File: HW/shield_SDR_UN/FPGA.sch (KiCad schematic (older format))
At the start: 0 parts

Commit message: Se añade el esquema de la FPGA
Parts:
- added C? (x18): 0.1uF, symbol Device:C
- added C? (x10): 4.7uF, symbol Device:C
- added D?: LED, symbol Device:LED
- added J?: Conn_02x18_Counter_Clockwise, symbol Connector_Generic:Conn_02x18_Counter_Clockwise
- added R?: R, symbol Device:R
- added U?: 6SLX9TQG144, symbol 6slx9tqg144:6SLX9TQG144
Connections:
- net labels added: +1V2, +3.3V, ADDR_DATA_MCU, ADD_DAT_00, ADD_DAT_01, ADD_DAT_02, ADD_DAT_03, ADD_DAT_04, ADD_DAT_05, ADD_DAT_06, ADD_DAT_07, ADD_DAT_08, ADD_DAT_09, ADD_DAT_10, ADD_DAT_11, ADD_DAT_12, ADD_DAT_13, ADD_DAT_14, ADD_DAT_15, ADD_DAT_16, ADD_DAT_17, ADD_DAT_18, ADD_DAT_19, ADD_DAT_20, ADD_DAT_21, ADD_DAT_22, ADD_DAT_23, ADD_DAT_24, ADD_DAT_25, ADD_DAT_26, ADD_DAT_27, ADD_DAT_28, ADD_DAT_29, ADD_DAT_30, ADD_DAT_31, BLK_LED, CLK_INPUT, CTRL_MCU, FPGA_GPIO_00, FPGA_GPIO_01, FPGA_GPIO_02, FPGA_GPIO_03, FPGA_GPIO_04, FPGA_GPIO_05, FPGA_GPIO_06, FPGA_GPIO_07, FPGA_GPIO_08, FPGA_GPIO_09, FPGA_GPIO_10, FPGA_GPIO_11, FPGA_GPIO_12, FPGA_GPIO_13, FPGA_GPIO_14, FPGA_GPIO_15, FPGA_GPIO_16, FPGA_GPIO_17, FPGA_GPIO_18, FPGA_GPIO_19, FPGA_GPIO_20, FPGA_GPIO_21, FPGA_GPIO_22, FPGA_GPIO_23, FPGA_GPIO_24, FPGA_GPIO_25, FPGA_GPIO_26, FPGA_GPIO_27, FPGA_GPIO_28, FPGA_GPIO_29, FPGA_GPIO_30, FPGA_GPIO_31, GND, SCL_I2C, SDA_I2C, START_MCU, TCK_FPGA, TDI_FPGA, TDO_FPGA, TMS_FPGA
- wire segments 0 -> 290
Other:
- note added: "Blink LED"
- note added: "Bus de datos y dirección\npara comunicación con\nel MCU"
- note added: "Espacio para memoria\n(si se requiere)"
- note added: "FPGA"
- note added: "Pines GPIO"

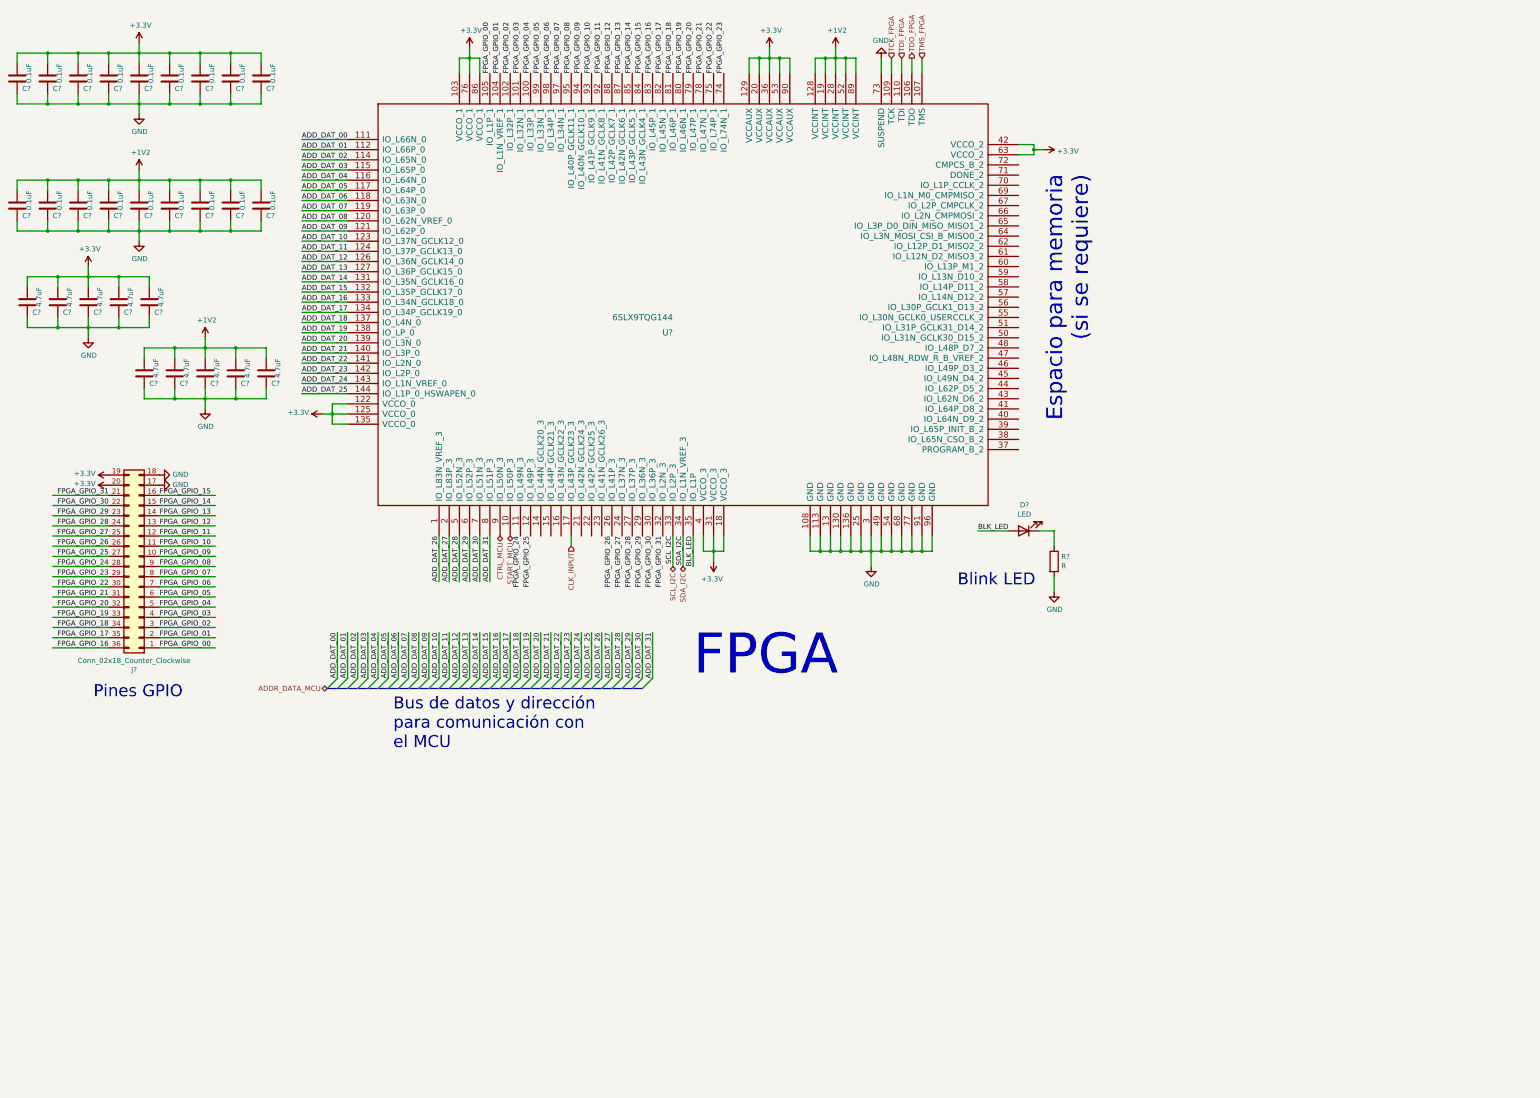
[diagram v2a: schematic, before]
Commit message: FPGA-ADC connection
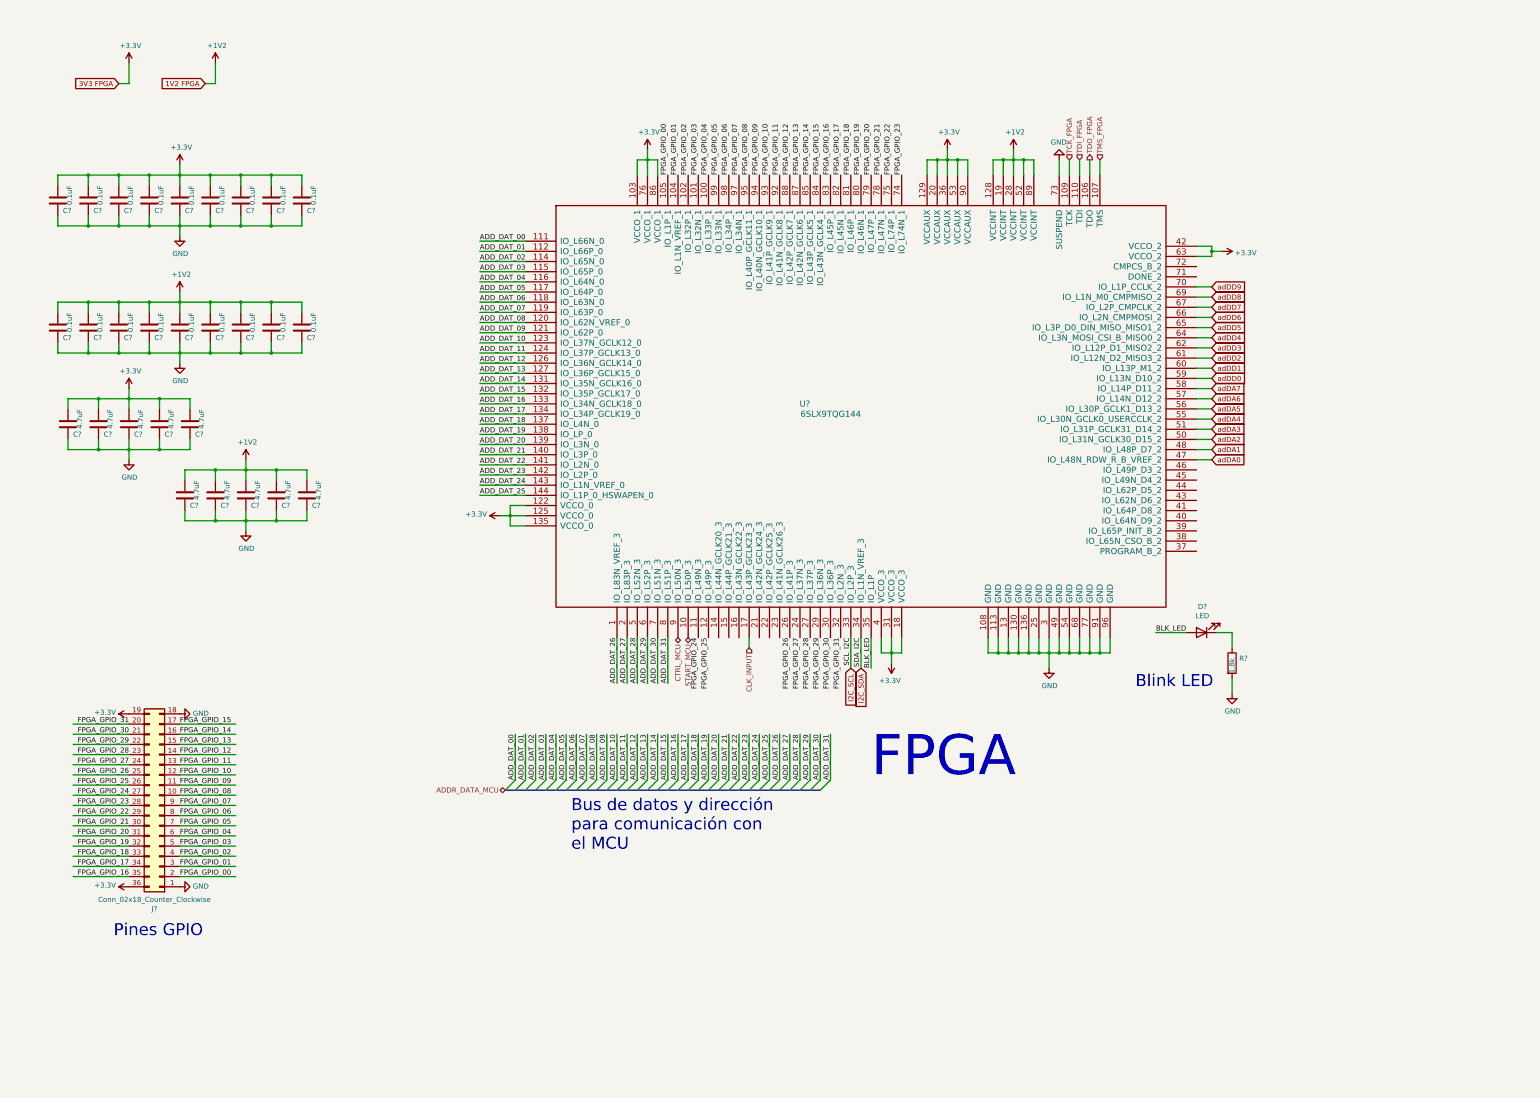
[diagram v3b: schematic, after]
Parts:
- R?: value R -> 1.8k
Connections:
- net labels added: 1V2 FPGA, 3V3 FPGA, I2C_SCL, I2C_SDA, adDA0, adDA1, adDA2, adDA3, adDA4, adDA5, adDA6, adDA7, adDD0, adDD1, adDD2, adDD3, adDD4, adDD5, adDD6, adDD7, adDD8, adDD9
- wire segments 290 -> 312
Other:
- note removed: "Espacio para memoria\n(si se requiere)"
- moved on the sheet: C?, D?, J?, R?, U?

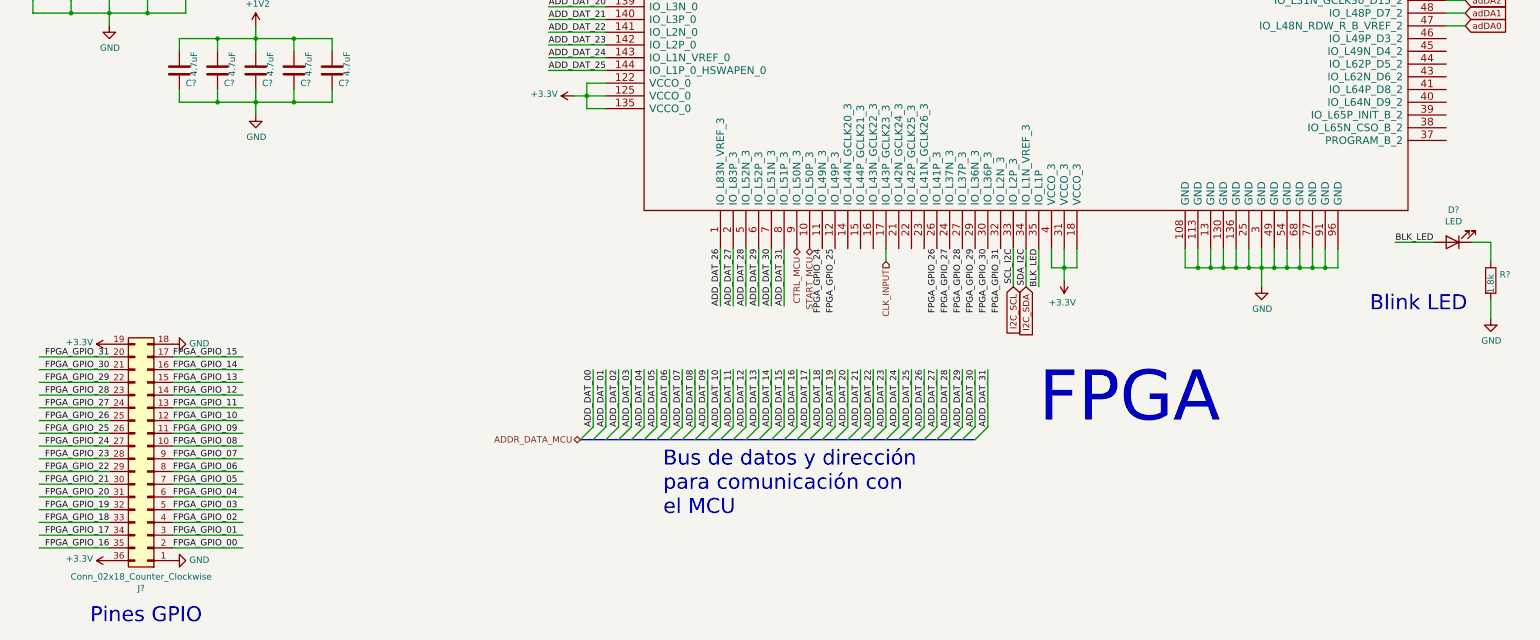
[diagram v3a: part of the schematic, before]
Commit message: STM32 connection updated
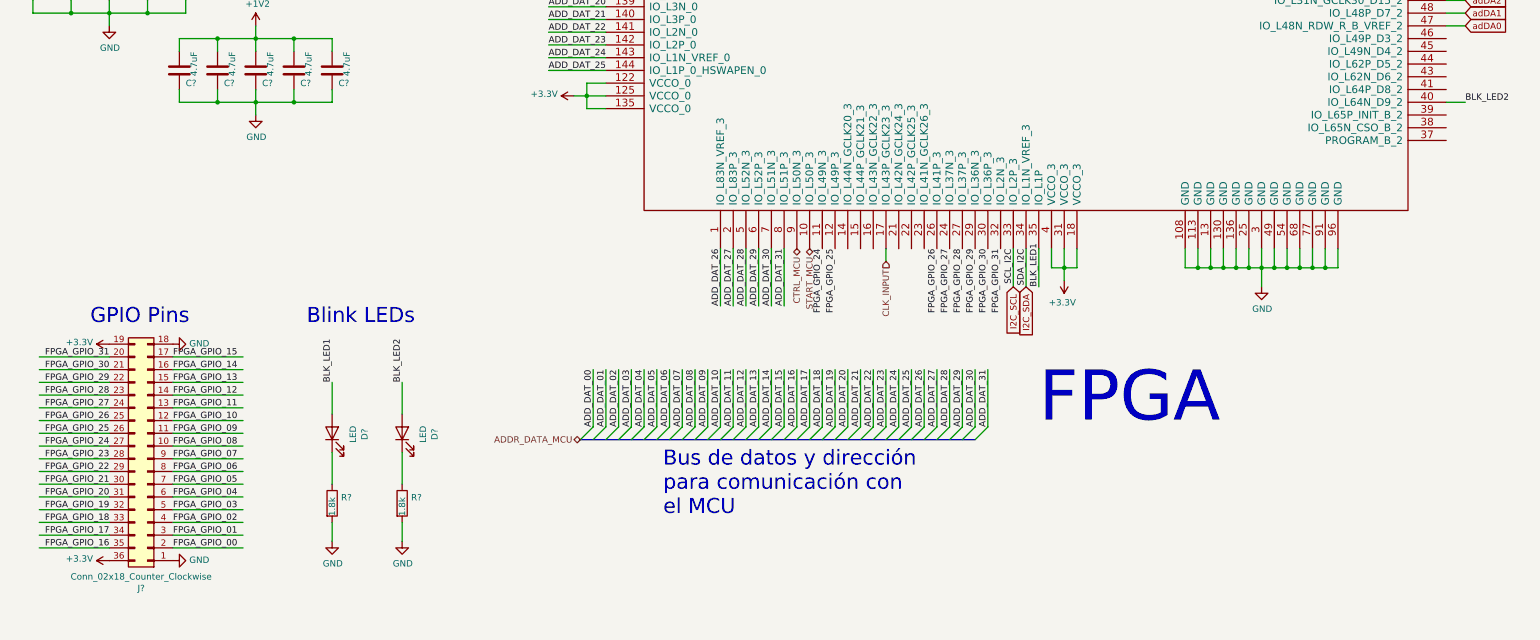
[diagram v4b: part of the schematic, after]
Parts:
- removed D?: LED, symbol Device:LED
- added D? (x2): LED, symbol Device:LED
- added R?: 1.8k, symbol Device:R
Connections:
- net labels added: BLK_LED1, BLK_LED2
- net labels removed: BLK_LED
- wire segments 312 -> 315
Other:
- note added: "Blink LEDs"
- note added: "GPIO Pins"
- note removed: "Blink LED"
- note removed: "Pines GPIO"
- moved on the sheet: R?
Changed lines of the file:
@@
 Text Label 8900 6650 3    50   ~ 0
 SDA_I2C
-Text Label 9000 6650 3    50   ~ 0
-BLK_LED
 Wire Wire Line
 	9000 6650 9000 6950
-Wire Wire Line
-	11800 6600 12100 6600
-$Comp
-L Device:LED D?
-U 1 1 5D3F3423
-P 12250 6600
-F 0 "D?" H 12242 6345 50  0000 C CNN
-F 1 "LED" H 12242 6436 50  0000 C CNN
-F 2 "" H 12250 6600 50  0001 C CNN
-F 3 "~" H 12250 6600 50  0001 C CNN
-	1    12250 6600
-	-1   0    0    1
-$EndComp
 $Comp
 L Device:R R?
 U 1 1 5D3F355A
-P 12550 6900
-F 0 "R?" H 12620 6946 50  0000 L CNN
-F 1 "1.8k" V 12550 6800 50  0000 L CNN
-F 2 "" V 12480 6900 50  0001 C CNN
-F 3 "~" H 12550 6900 50  0001 C CNN
-	1    12550 6900
-	1    0    0    -1
-$EndComp
-Wire Wire Line
-	12550 6750 12550 6600
-Wire Wire Line
-	12400 6600 12550 6600
+P 3450 8650
+F 0 "R?" H 3520 8696 50  0000 L CNN
+F 1 "1.8k" V 3450 8550 50  0000 L CNN
+F 2 "" V 3380 8650 50  0001 C CNN
+F 3 "~" H 3450 8650 50  0001 C CNN
+	1    3450 8650
+	1    0    0    -1
+$EndComp
 $Comp
 L power:GND #PWR?
 U 1 1 5D40658F
-P 12550 7200
-F 0 "#PWR?" H 12550 6950 50  0001 C CNN
-F 1 "GND" H 12555 7027 50  0000 C CNN
-F 2 "" H 12550 7200 50  0001 C CNN
-F 3 "" H 12550 7200 50  0001 C CNN
-	1    12550 7200
-	1    0    0    -1
-$EndComp
-Wire Wire Line
-	12550 7050 12550 7200
-Text Label 12100 6600 2    50   ~ 0
-BLK_LED
+P 3450 8950
+F 0 "#PWR?" H 3450 8700 50  0001 C CNN
+F 1 "GND" H 3455 8777 50  0000 C CNN
+F 2 "" H 3450 8950 50  0001 C CNN
+F 3 "" H 3450 8950 50  0001 C CNN
+	1    3450 8950
+	1    0    0    -1
+$EndComp
+Wire Wire Line
+	3450 8800 3450 8950
+Text Label 3450 7700 1    50   ~ 0
+BLK_LED1
 Wire Wire Line
 	8900 6650 8900 6950
@@
 Text Notes 9000 8050 0    394  ~ 0
 FPGA
-Text Notes 11600 7150 0    118  ~ 0
-Blink LED
+Text Notes 3250 7250 0    118  ~ 0
+Blink LEDs
 Wire Wire Line
 	5150 4350 5600 4350
 Text Notes 6050 8750 0    118  ~ 0
 Bus de datos y dirección\npara comunicación con\nel MCU
-Text Notes 1550 9600 0    118  ~ 0
-Pines GPIO
+Text Notes 1550 7250 0    118  ~ 0
+GPIO Pins
 Text GLabel 8800 6950 3    50   Input ~ 0
 I2C_SCL
@@
 Wire Wire Line
 	2550 1200 2550 1000
+$Comp
+L Device:LED D?
+U 1 1 5D23F274
+P 3450 8100
+F 0 "D?" H 3442 7845 50  0000 C CNN
+F 1 "LED" H 3442 7936 50  0000 C CNN
+F 2 "" H 3450 8100 50  0001 C CNN
+F 3 "~" H 3450 8100 50  0001 C CNN
+	1    3450 8100
+	0    -1   -1   0
+$EndComp
+Wire Wire Line
+	3450 7700 3450 7950
+Wire Wire Line
+	3450 8250 3450 8500
+$Comp
+L Device:R R?
+U 1 1 5D398B89
+P 4000 8650
+F 0 "R?" H 4070 8696 50  0000 L CNN
+F 1 "1.8k" V 4000 8550 50  0000 L CNN
+F 2 "" V 3930 8650 50  0001 C CNN
+F 3 "~" H 4000 8650 50  0001 C CNN
+	1    4000 8650
+	1    0    0    -1
+$EndComp
+$Comp
+L power:GND #PWR?
+U 1 1 5D398B91
+P 4000 8950
+F 0 "#PWR?" H 4000 8700 50  0001 C CNN
+F 1 "GND" H 4005 8777 50  0000 C CNN
+F 2 "" H 4000 8950 50  0001 C CNN
+F 3 "" H 4000 8950 50  0001 C CNN
+	1    4000 8950
+	1    0    0    -1
+$EndComp
+Wire Wire Line
+	4000 8800 4000 8950
+Text Label 4000 7700 1    50   ~ 0
+BLK_LED2
+$Comp
+L Device:LED D?
+U 1 1 5D398B9D
+P 4000 8100
+F 0 "D?" H 3992 7845 50  0000 C CNN
+F 1 "LED" H 3992 7936 50  0000 C CNN
+F 2 "" H 4000 8100 50  0001 C CNN
+F 3 "~" H 4000 8100 50  0001 C CNN
+	1    4000 8100
+	0    -1   -1   0
+$EndComp
+Wire Wire Line
+	4000 7700 4000 7950
+Wire Wire Line
+	4000 8250 4000 8500
+Text Label 9000 6950 1    50   ~ 0
+BLK_LED1
+Text Label 12350 5500 0    50   ~ 0
+BLK_LED2
+Wire Wire Line
+	12350 5500 12200 5500
 Wire Bus Line
 	5400 8150 8500 8150

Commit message: data bus proc-fpga
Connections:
- net labels added: PROC-FPGA [0:14]
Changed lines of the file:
@@
 Entry Wire Line
 	6800 8150 6900 8050
-Entry Wire Line
-	6900 8150 7000 8050
-Entry Wire Line
-	7000 8150 7100 8050
-Entry Wire Line
-	7100 8150 7200 8050
-Entry Wire Line
-	7200 8150 7300 8050
-Entry Wire Line
-	7300 8150 7400 8050
-Entry Wire Line
-	7400 8150 7500 8050
-Entry Wire Line
-	7500 8150 7600 8050
-Entry Wire Line
-	7600 8150 7700 8050
-Entry Wire Line
-	7700 8150 7800 8050
-Entry Wire Line
-	7800 8150 7900 8050
-Entry Wire Line
-	7900 8150 8000 8050
 Wire Wire Line
 	5500 8050 5500 7600
@@
 Wire Wire Line
 	6900 8050 6900 7600
-Wire Wire Line
-	7000 8050 7000 7600
-Wire Wire Line
-	7100 8050 7100 7600
-Wire Wire Line
-	7200 8050 7200 7600
-Wire Wire Line
-	7300 8050 7300 7600
-Wire Wire Line
-	7400 8050 7400 7600
-Wire Wire Line
-	7500 8050 7500 7600
-Wire Wire Line
-	7600 8050 7600 7600
-Wire Wire Line
-	7700 8050 7700 7600
-Wire Wire Line
-	7800 8050 7800 7600
-Wire Wire Line
-	7900 8050 7900 7600
-Wire Wire Line
-	8000 8050 8000 7600
 Text Label 5500 8050 1    50   ~ 0
 ADD_DAT_00
@@
 Text Label 6900 8050 1    50   ~ 0
 ADD_DAT_14
-Text Label 7000 8050 1    50   ~ 0
-ADD_DAT_15
-Text Label 7100 8050 1    50   ~ 0
-ADD_DAT_16
-Text Label 7200 8050 1    50   ~ 0
-ADD_DAT_17
-Text Label 7300 8050 1    50   ~ 0
-ADD_DAT_18
-Text Label 7400 8050 1    50   ~ 0
-ADD_DAT_19
-Text Label 7500 8050 1    50   ~ 0
-ADD_DAT_20
-Text Label 7600 8050 1    50   ~ 0
-ADD_DAT_21
-Text Label 7700 8050 1    50   ~ 0
-ADD_DAT_22
-Text Label 7800 8050 1    50   ~ 0
-ADD_DAT_23
-Text Label 7900 8050 1    50   ~ 0
-ADD_DAT_24
-Text Label 8000 8050 1    50   ~ 0
-ADD_DAT_25
-Entry Wire Line
-	8000 8150 8100 8050
-Entry Wire Line
-	8100 8150 8200 8050
-Entry Wire Line
-	8200 8150 8300 8050
-Entry Wire Line
-	8300 8150 8400 8050
-Entry Wire Line
-	8400 8150 8500 8050
-Entry Wire Line
-	8500 8150 8600 8050
-Wire Wire Line
-	8100 8050 8100 7600
-Text Label 8100 8050 1    50   ~ 0
-ADD_DAT_26
-Wire Wire Line
-	8200 8050 8200 7600
-Text Label 8200 8050 1    50   ~ 0
-ADD_DAT_27
-Wire Wire Line
-	8300 8050 8300 7600
-Text Label 8300 8050 1    50   ~ 0
-ADD_DAT_28
-Wire Wire Line
-	8400 8050 8400 7600
-Text Label 8400 8050 1    50   ~ 0
-ADD_DAT_29
-Wire Wire Line
-	8500 8050 8500 7600
-Text Label 8500 8050 1    50   ~ 0
-ADD_DAT_30
-Wire Wire Line
-	8600 8050 8600 7600
-Text Label 8600 8050 1    50   ~ 0
-ADD_DAT_31
-Text HLabel 5400 8150 0    50   BiDi ~ 0
-ADDR_DATA_MCU
 Text HLabel 7200 6650 3    50   BiDi ~ 0
 START_MCU
@@
 Wire Wire Line
 	5150 4350 5600 4350
-Text Notes 6050 8750 0    118  ~ 0
+Text Notes 5400 10600 0    118  ~ 0
 Bus de datos y dirección\npara comunicación con\nel MCU
 Text Notes 1550 7250 0    118  ~ 0
@@
 Wire Wire Line
 	12350 5500 12200 5500
+Text GLabel 5300 8150 0    50   Input ~ 0
+PROC-FPGA [0:14]
+Entry Wire Line
+	5850 9350 5950 9450
+Entry Wire Line
+	5950 9350 6050 9450
+Entry Wire Line
+	6050 9350 6150 9450
+Entry Wire Line
+	6150 9350 6250 9450
+Entry Wire Line
+	6250 9350 6350 9450
+Entry Wire Line
+	6350 9350 6450 9450
+Entry Wire Line
+	6450 9350 6550 9450
+Entry Wire Line
+	6550 9350 6650 9450
+Entry Wire Line
+	6650 9350 6750 9450
+Entry Wire Line
+	6750 9350 6850 9450
+Entry Wire Line
+	6850 9350 6950 9450
+Wire Wire Line
+	5950 9450 5950 9900
+Wire Wire Line
+	6050 9450 6050 9900
+Wire Wire Line
+	6150 9450 6150 9900
+Wire Wire Line
+	6250 9450 6250 9900
+Wire Wire Line
+	6350 9450 6350 9900
+Wire Wire Line
+	6450 9450 6450 9900
+Wire Wire Line
+	6550 9450 6550 9900
+Wire Wire Line
+	6650 9450 6650 9900
+Wire Wire Line
+	6750 9450 6750 9900
+Wire Wire Line
+	6850 9450 6850 9900
+Wire Wire Line
+	6950 9450 6950 9900
+Text Label 5950 9900 1    50   ~ 0
+ADD_DAT_15
+Text Label 6150 9900 1    50   ~ 0
+ADD_DAT_17
+Text Label 6250 9900 1    50   ~ 0
+ADD_DAT_18
+Text Label 6350 9900 1    50   ~ 0
+ADD_DAT_19
+Text Label 6450 9900 1    50   ~ 0
+ADD_DAT_20
+Text Label 6550 9900 1    50   ~ 0
+ADD_DAT_21
+Text Label 6650 9900 1    50   ~ 0
+ADD_DAT_22
+Text Label 6750 9900 1    50   ~ 0
+ADD_DAT_23
+Text Label 6850 9900 1    50   ~ 0
+ADD_DAT_24
+Text Label 6950 9900 1    50   ~ 0
+ADD_DAT_25
+Entry Wire Line
+	6950 9350 7050 9450
+Entry Wire Line
+	7050 9350 7150 9450
+Entry Wire Line
+	7150 9350 7250 9450
+Entry Wire Line
+	7250 9350 7350 9450
+Entry Wire Line
+	7350 9350 7450 9450
+Entry Wire Line
+	7450 9350 7550 9450
+Wire Wire Line
+	7050 9450 7050 9900
+Text Label 7050 9900 1    50   ~ 0
+ADD_DAT_26
+Wire Wire Line
+	7150 9450 7150 9900
+Text Label 7150 9900 1    50   ~ 0
+ADD_DAT_27
+Wire Wire Line
+	7250 9450 7250 9900
+Text Label 7250 9900 1    50   ~ 0
+ADD_DAT_28
+Wire Wire Line
+	7350 9450 7350 9900
+Text Label 7350 9900 1    50   ~ 0
+ADD_DAT_29
+Wire Wire Line
+	7450 9450 7450 9900
+Text Label 7450 9900 1    50   ~ 0
+ADD_DAT_30
+Wire Wire Line
+	7550 9450 7550 9900
+Text Label 7550 9900 1    50   ~ 0
+ADD_DAT_31
+Text GLabel 5700 9350 0    50   Input ~ 0
+ADDR_DATA_MCU
+Text Label 6050 9900 1    50   ~ 0
+ADD_DAT_16
 Wire Bus Line
-	5400 8150 8500 8150
+	5300 8150 6800 8150
+Wire Bus Line
+	5700 9350 7450 9350
 $EndSCHEMATC

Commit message: bus-v2 proc-fpga
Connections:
- net labels added: FMC_A14, FMC_A15, FMC_A16, FMC_A17, FMC_A18, FMC_A19, FMC_A20, FMC_A21, FMC_A22, FMC_A23, FMC_CLK, FMC_D0, FMC_D1, FMC_D10, FMC_D11, FMC_D12, FMC_D13, FMC_D14, FMC_D15, FMC_D2, FMC_D3, FMC_D4, FMC_D5, FMC_D6, FMC_D7, FMC_D8, FMC_D9, FMC_NE1, FMC_NL, FMC_NOE, FMC_NWAIT, FMC_NWE, PROC-FPGA_FMC_D [0:15], PROC_FPGA_FMC_A[14:23], PROC_FPGA_FMC_C [0:5]
- net labels removed: ADDR_DATA_MCU, ADD_DAT_00, ADD_DAT_01, ADD_DAT_02, ADD_DAT_03, ADD_DAT_04, ADD_DAT_05, ADD_DAT_06, ADD_DAT_07, ADD_DAT_08, ADD_DAT_09, ADD_DAT_10, ADD_DAT_11, ADD_DAT_12, ADD_DAT_13, ADD_DAT_14, ADD_DAT_15, ADD_DAT_16, ADD_DAT_17, ADD_DAT_18, ADD_DAT_19, ADD_DAT_20, ADD_DAT_21, ADD_DAT_22, ADD_DAT_23, ADD_DAT_24, ADD_DAT_25, ADD_DAT_26, ADD_DAT_27, ADD_DAT_28, ADD_DAT_29, ADD_DAT_30, ADD_DAT_31, PROC-FPGA [0:14]
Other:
- note added: "BUS DATA-ADDRESS-CONTROL \nPROC<->FPGA\n"
- note added: "FMC_NADV o NL\n"
- note removed: "Bus de datos y dirección\npara comunicación con\nel MCU"
